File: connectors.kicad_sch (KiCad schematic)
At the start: 4 parts, among them J1 Conn_01x04_Pin, J2 Conn_01x04_Pin, J3 Conn_01x09_Pin, J4 Conn_02x03_Odd_Even

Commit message: Completed symbols to footprint association
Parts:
- J1, J2: footprint TQFP32_32A_MCH -> Connector_PinHeader_2.54mm:PinHeader_1x04_P2.54mm_Vertical
- J3: footprint (none) -> Connector_PinHeader_2.54mm:PinHeader_1x09_P2.54mm_Vertical
- J4: footprint (none) -> Connector_PinHeader_2.54mm:PinHeader_2x03_P2.54mm_Vertical
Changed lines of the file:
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@@
 			)
 		)
-		(property "Footprint" ""
+		(property "Footprint" "Connector_PinHeader_2.54mm:PinHeader_2x03_P2.54mm_Vertical"
 			(at 127 132.08 0)
 			(hide yes)
@@
 			)
 		)
-		(property "Footprint" "TQFP32_32A_MCH"
+		(property "Footprint" "Connector_PinHeader_2.54mm:PinHeader_1x04_P2.54mm_Vertical"
 			(at 101.6 107.95 0)
 			(hide yes)
@@
 			)
 		)
-		(property "Footprint" ""
+		(property "Footprint" "Connector_PinHeader_2.54mm:PinHeader_1x09_P2.54mm_Vertical"
 			(at 101.6 143.51 0)
 			(hide yes)
@@
 			)
 		)
-		(property "Footprint" "TQFP32_32A_MCH"
+		(property "Footprint" "Connector_PinHeader_2.54mm:PinHeader_1x04_P2.54mm_Vertical"
 			(at 120.65 106.68 0)
 			(hide yes)

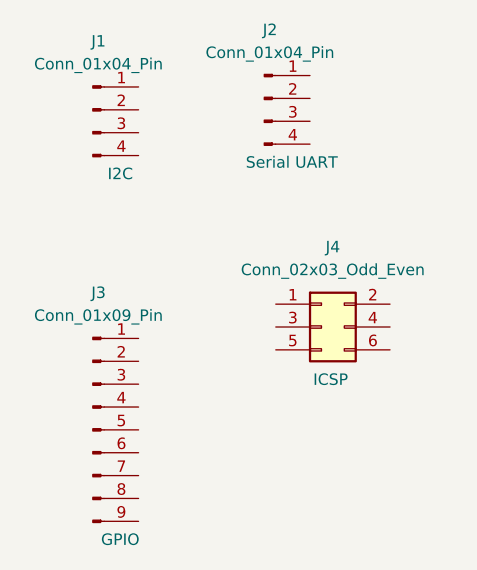
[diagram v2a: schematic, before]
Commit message: Completed wiring
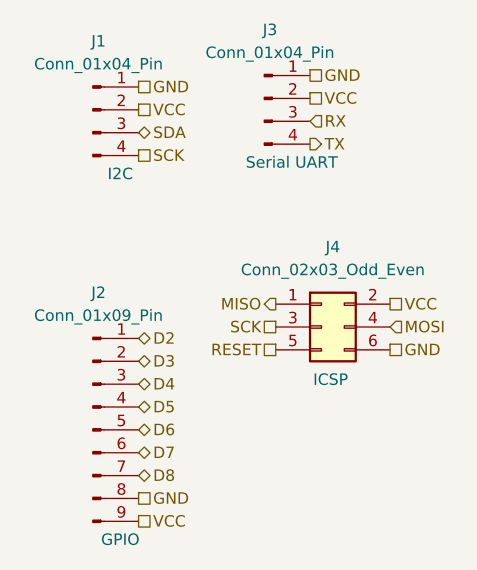
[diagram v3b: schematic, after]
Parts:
- renumbered J3 to J2, J2 to J3
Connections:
- net MISO: now reaches J4.1 (Pin_1)
- net VCC: now reaches J4.2 (Pin_2)
- net VCC: now also J1.2 (Pin_2), J2.9 (Pin_9), J3.2 (Pin_2)
- net SCK: now reaches J4.3 (Pin_3)
- net SCK: now also J1.4 (Pin_4)
- net MOSI: now reaches J4.4 (Pin_4)
- net RESET: now reaches J4.5 (Pin_5)
- net GND: now reaches J4.6 (Pin_6)
- net GND: now also J1.1 (Pin_1), J2.8 (Pin_8), J3.1 (Pin_1)
- net SDA: now reaches J1.3 (Pin_3)
- net D2: now reaches J2.1 (Pin_1)
- net D3: now reaches J2.2 (Pin_2)
- net D4: now reaches J2.3 (Pin_3)
- net D5: now reaches J2.4 (Pin_4)
- net D6: now reaches J2.5 (Pin_5)
- net D7: now reaches J2.6 (Pin_6)
- net D8: now reaches J2.7 (Pin_7)
- net RX: now reaches J3.3 (Pin_3)
- net TX: now reaches J3.4 (Pin_4)
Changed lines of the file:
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@@
 	(generator_version "10.0")
 	(paper "A4")
+	(hierarchical_label "D6"
+		(shape bidirectional)
+		(at 106.68 143.51 0)
+		(effects
+			(font
+				(size 1.27 1.27)
+			)
+			(justify left)
+		)
+	)
+	(hierarchical_label "D2"
+		(shape bidirectional)
+		(at 106.68 133.35 0)
+		(effects
+			(font
+				(size 1.27 1.27)
+			)
+			(justify left)
+		)
+	)
+	(hierarchical_label "VCC"
+		(shape passive)
+		(at 125.73 106.68 0)
+		(effects
+			(font
+				(size 1.27 1.27)
+			)
+			(justify left)
+		)
+	)
+	(hierarchical_label "RESET"
+		(shape passive)
+		(at 121.92 134.62 180)
+		(effects
+			(font
+				(size 1.27 1.27)
+			)
+			(justify right)
+		)
+	)
+	(hierarchical_label "RX"
+		(shape input)
+		(at 125.73 109.22 0)
+		(effects
+			(font
+				(size 1.27 1.27)
+			)
+			(justify left)
+		)
+	)
+	(hierarchical_label "VCC"
+		(shape passive)
+		(at 106.68 107.95 0)
+		(effects
+			(font
+				(size 1.27 1.27)
+			)
+			(justify left)
+		)
+	)
+	(hierarchical_label "GND"
+		(shape passive)
+		(at 134.62 134.62 0)
+		(effects
+			(font
+				(size 1.27 1.27)
+			)
+			(justify left)
+		)
+	)
+	(hierarchical_label "D8"
+		(shape bidirectional)
+		(at 106.68 148.59 0)
+		(effects
+			(font
+				(size 1.27 1.27)
+			)
+			(justify left)
+		)
+	)
+	(hierarchical_label "MOSI"
+		(shape input)
+		(at 134.62 132.08 0)
+		(effects
+			(font
+				(size 1.27 1.27)
+			)
+			(justify left)
+		)
+	)
+	(hierarchical_label "TX"
+		(shape output)
+		(at 125.73 111.76 0)
+		(effects
+			(font
+				(size 1.27 1.27)
+			)
+			(justify left)
+		)
+	)
+	(hierarchical_label "SDA"
+		(shape bidirectional)
+		(at 106.68 110.49 0)
+		(effects
+			(font
+				(size 1.27 1.27)
+			)
+			(justify left)
+		)
+	)
+	(hierarchical_label "MISO"
+		(shape output)
+		(at 121.92 129.54 180)
+		(effects
+			(font
+				(size 1.27 1.27)
+			)
+			(justify right)
+		)
+	)
+	(hierarchical_label "GND"
+		(shape passive)
+		(at 106.68 151.13 0)
+		(effects
+			(font
+				(size 1.27 1.27)
+			)
+			(justify left)
+		)
+	)
+	(hierarchical_label "GND"
+		(shape passive)
+		(at 125.73 104.14 0)
+		(effects
+			(font
+				(size 1.27 1.27)
+			)
+			(justify left)
+		)
+	)
+	(hierarchical_label "SCK"
+		(shape passive)
+		(at 106.68 113.03 0)
+		(effects
+			(font
+				(size 1.27 1.27)
+			)
+			(justify left)
+		)
+	)
+	(hierarchical_label "D7"
+		(shape bidirectional)
+		(at 106.68 146.05 0)
+		(effects
+			(font
+				(size 1.27 1.27)
+			)
+			(justify left)
+		)
+	)
+	(hierarchical_label "D5"
+		(shape bidirectional)
+		(at 106.68 140.97 0)
+		(effects
+			(font
+				(size 1.27 1.27)
+			)
+			(justify left)
+		)
+	)
+	(hierarchical_label "VCC"
+		(shape passive)
+		(at 106.68 153.67 0)
+		(effects
+			(font
+				(size 1.27 1.27)
+			)
+			(justify left)
+		)
+	)
+	(hierarchical_label "D3"
+		(shape bidirectional)
+		(at 106.68 135.89 0)
+		(effects
+			(font
+				(size 1.27 1.27)
+			)
+			(justify left)
+		)
+	)
+	(hierarchical_label "VCC"
+		(shape passive)
+		(at 134.62 129.54 0)
+		(effects
+			(font
+				(size 1.27 1.27)
+			)
+			(justify left)
+		)
+	)
+	(hierarchical_label "SCK"
+		(shape passive)
+		(at 121.92 132.08 180)
+		(effects
+			(font
+				(size 1.27 1.27)
+			)
+			(justify right)
+		)
+	)
+	(hierarchical_label "GND"
+		(shape passive)
+		(at 106.68 105.41 0)
+		(effects
+			(font
+				(size 1.27 1.27)
+			)
+			(justify left)
+		)
+	)
+	(hierarchical_label "D4"
+		(shape bidirectional)
+		(at 106.68 138.43 0)
+		(effects
+			(font
+				(size 1.27 1.27)
+			)
+			(justify left)
+		)
+	)
 	(symbol
 		(lib_id "Connector_Generic:Conn_02x03_Odd_Even")
@@
 		(in_pos_files yes)
 		(dnp no)
-		(property "Reference" "J3"
+		(property "Reference" "J2"
 			(at 102.235 128.27 0)
 			(show_name no)
@@
 			(project "MCU Datalogger"
 				(path "/455fe25c-2e84-4f23-ad2d-4a44fcc92110/5572c0ca-da16-4cc5-93f1-4f24fcba599c"
-					(reference "J3")
+					(reference "J2")
 					(unit 1)
 				)
@@
 		(in_pos_files yes)
 		(dnp no)
-		(property "Reference" "J2"
+		(property "Reference" "J3"
 			(at 121.285 99.06 0)
 			(show_name no)
@@
 			(project "MCU Datalogger"
 				(path "/455fe25c-2e84-4f23-ad2d-4a44fcc92110/5572c0ca-da16-4cc5-93f1-4f24fcba599c"
-					(reference "J2")
+					(reference "J3")
 					(unit 1)
 				)
